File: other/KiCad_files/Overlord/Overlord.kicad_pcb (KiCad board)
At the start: 2 copper layers, 155.7 x 86.3 mm, 230 parts, among them IC1 74HC4052D,653, IC2 74HC4052D,653, IC3 74HC4052D,653, IC4 74HC4052D,653, J1 39502-1011, J2 39502-1011, J3 39502-1011, J4 Conn_01x12_Pin, J5 Conn_01x10_Pin, J6 Conn_01x11_Pin, J7 Conn_01x11_Pin, J8 Conn_01x04_Pin, J9 Conn_01x04_Pin

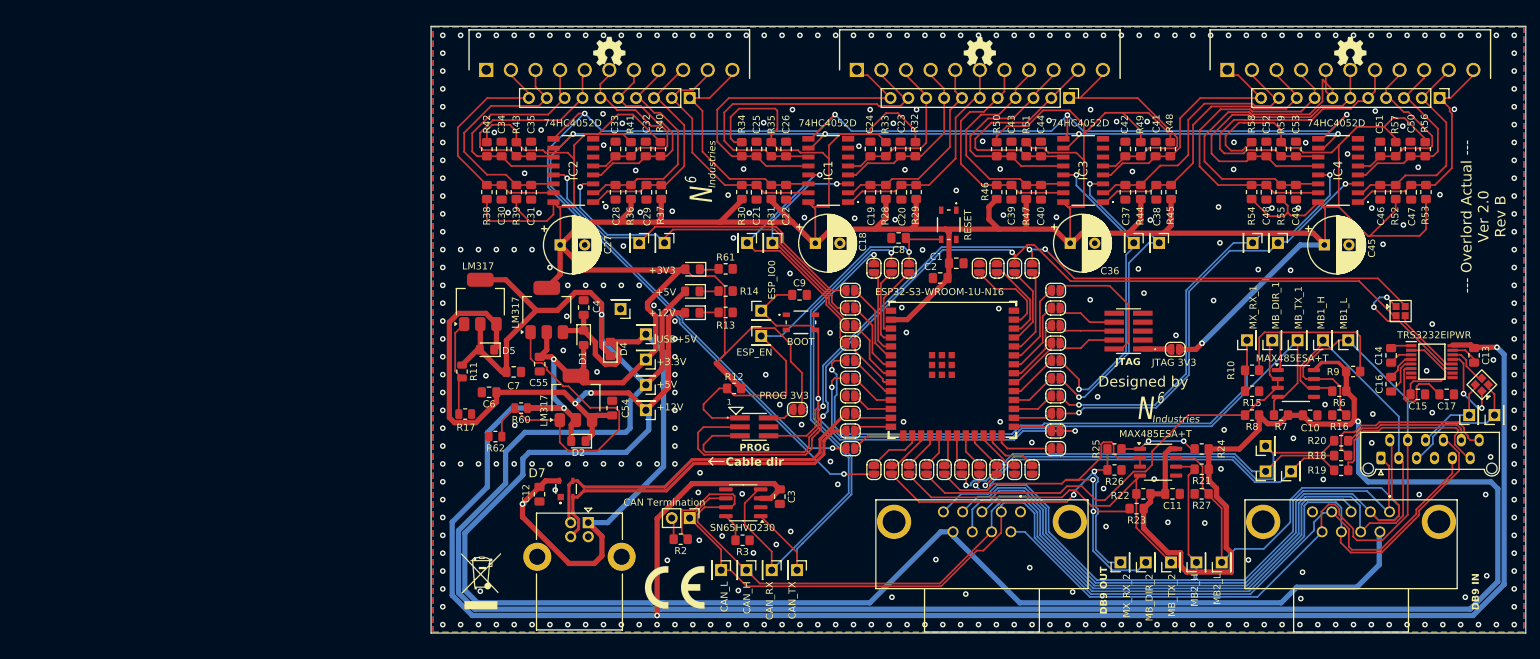
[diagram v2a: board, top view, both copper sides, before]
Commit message: Sent for PCB production, ver 2.1 rev A
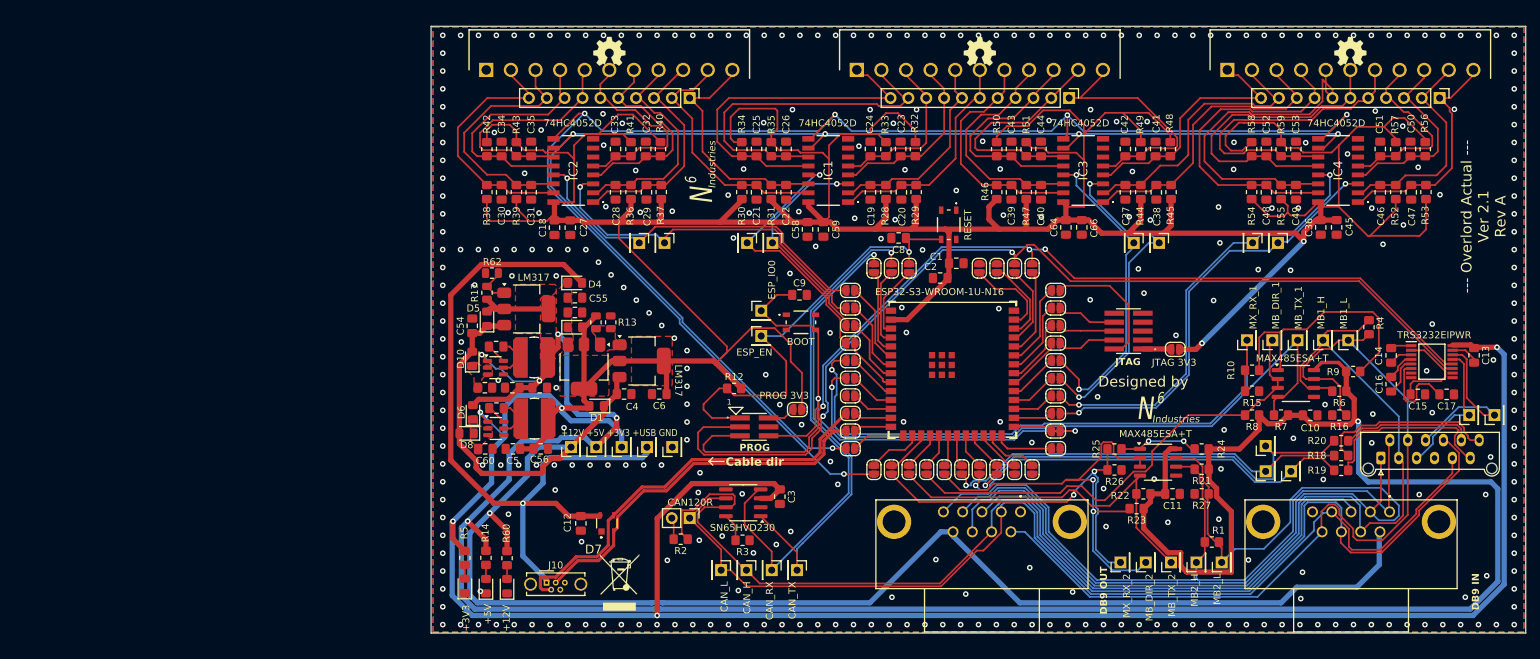
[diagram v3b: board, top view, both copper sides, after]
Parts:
- removed 3V3LED2: LED, LED_SMD:LED_0805_2012Metric_Pad1.15x1.40mm_HandSolder
- removed J8, J9: Conn_01x04_Pin, OverlordCommon:Solder_select_2x2
- removed J_USB1: USB_B, OverlordCommon:USB
- removed R61: 60, Resistor_SMD:R_0805_2012Metric_Pad1.20x1.40mm_HandSolder
- removed SYM7: CE, Symbol:CE-Logo_8.5x6mm_SilkScreen
- added 3V3LED1: LED, LED_SMD:LED_0805_2012Metric_Pad1.15x1.40mm_HandSolder, F.Cu at (29.9, 104.9)
- added C5: 22uF, Capacitor_SMD:C_0805_2012Metric_Pad1.18x1.45mm_HandSolder, F.Cu at (36.7, 85.4)
- added C56: 22uF, Capacitor_SMD:C_0805_2012Metric_Pad1.18x1.45mm_HandSolder, F.Cu at (40.7, 85.4)
- added C57: 0.1uF, Capacitor_SMD:C_0805_2012Metric_Pad1.18x1.45mm_HandSolder, F.Cu at (34.4, 79.6)
- added C58: 0.1uF, Capacitor_SMD:C_0805_2012Metric_Pad1.18x1.45mm_HandSolder, F.Cu at (78.6, 54.2)
- added C59: 10uF, Capacitor_SMD:C_0805_2012Metric_Pad1.18x1.45mm_HandSolder, F.Cu at (80.9, 54.2)
- added C60: 10uF, Capacitor_SMD:C_0805_2012Metric_Pad1.18x1.45mm_HandSolder, F.Cu at (32.8, 85.4)
- added C61: 22uF, Capacitor_SMD:C_0805_2012Metric_Pad1.18x1.45mm_HandSolder, F.Cu at (36.6, 76.7)
- added C62: 22uF, Capacitor_SMD:C_0805_2012Metric_Pad1.18x1.45mm_HandSolder, F.Cu at (40.5, 76.7)
- added C63: 0.1uF, Capacitor_SMD:C_0805_2012Metric_Pad1.18x1.45mm_HandSolder, F.Cu at (34.4, 70.8)
- added C64: 0.1uF, Capacitor_SMD:C_0805_2012Metric_Pad1.18x1.45mm_HandSolder, F.Cu at (115.4, 53.9)
- added C65: 10uF, Capacitor_SMD:C_0805_2012Metric_Pad1.18x1.45mm_HandSolder, F.Cu at (32.8, 76.7)
- added C66: 10uF, Capacitor_SMD:C_0805_2012Metric_Pad1.18x1.45mm_HandSolder, F.Cu at (117.7, 53.9)
- added D10: 1N4148, Diode_SMD:D_0805_2012Metric_Pad1.15x1.40mm_HandSolder, F.Cu at (30.9, 72.6)
- added D6: 1N4148, Diode_SMD:D_0805_2012Metric_Pad1.15x1.40mm_HandSolder, F.Cu at (31.1, 80.2)
- added D8: 1N4148, Diode_SMD:D_0805_2012Metric_Pad1.15x1.40mm_HandSolder, F.Cu at (30.1, 83.2)
- added J10: USB_B_Micro, Connector_USB:USB_Micro-B_Wuerth_614105150721_Vertical_CircularHoles, F.Cu at (41.5, 104.4)
- added L1: 3.9uH, Inductor_SMD:L_Bourns_SDR0604, F.Cu at (39.8, 81.1)
- added L2: 4.7uH, Inductor_SMD:L_Bourns_SDR0604, F.Cu at (39.8, 72.4)
- added R1: 499, Resistor_SMD:R_0805_2012Metric_Pad1.20x1.40mm_HandSolder, F.Cu at (136.2, 98.7)
- added R4: 499, Resistor_SMD:R_0805_2012Metric_Pad1.20x1.40mm_HandSolder, F.Cu at (158.5, 68.1)
- added R5: 60, Resistor_SMD:R_0805_2012Metric_Pad1.20x1.40mm_HandSolder, F.Cu at (29.9, 100.9)
- added U1: AP63203WU, Package_TO_SOT_SMD:TSOT-23-6, F.Cu at (34.3, 82.5)
- added U2: AP63205WU, Package_TO_SOT_SMD:TSOT-23-6, F.Cu at (34.2, 73.8)
- C18, C36: value 220uF -> 0.1uF; footprint Capacitor_THT:CP_Radial_D8.0mm_P3.50mm -> Capacitor_SMD:C_0805_2012Metric_Pad1.18x1.45mm_HandSolder
- C27, C45: value 220uF -> 10uF; footprint Capacitor_THT:CP_Radial_D8.0mm_P3.50mm -> Capacitor_SMD:C_0805_2012Metric_Pad1.18x1.45mm_HandSolder
- R13: value 499 -> 390; footprint Resistor_SMD:R_0805_2012Metric_Pad1.20x1.40mm_HandSolder -> Resistor_SMD:R_0805_2012Metric
- R17: value 680 -> 240
- R60: value 240 -> 499; footprint Resistor_SMD:R_0805_2012Metric -> Resistor_SMD:R_0805_2012Metric_Pad1.20x1.40mm_HandSolder
- R62: value 390 -> 680
- moved 5VLED1 51.2 mm to (32.9, 104.9), turned to 90 degrees
- moved R14 51.0 mm to (32.9, 100.9), turned to -90 degrees
- moved 12VLED1 47.0 mm to (35.9, 104.9), turned to 90 degrees
- moved C18 37.2 mm to (42.6, 53.9), turned to 90 degrees
- moved C36 35.7 mm to (151.6, 53.9), turned to 90 degrees
- moved C6 24.2 mm to (57.5, 77.6)
- moved R62 23.3 mm to (33.8, 60.4)
- moved C54 23.1 mm to (30.9, 67.9)
- moved R60 21.4 mm to (35.9, 101.0), turned to -90 degrees
- moved Dbg19 21.0 mm to (59.4, 85.2), turned to 90 degrees
- moved R11 20.3 mm to (48.5, 67.4)
- moved SYM6 19.7 mm to (51.9, 104.4)
- moved R17 17.5 mm to (33.0, 63.2), turned to 90 degrees
- moved U_LM317_2 17.4 mm to (46.9, 73.7), turned to -90 degrees
- moved R13 16.4 mm to (50.6, 67.4), turned to 90 degrees
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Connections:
- 12VLED1 pad 1: Net-(12VLED1-K) -> GND
- 12VLED1 pad 2: +12V -> Net-(12VLED1-A)
- 5VLED1 pad 1: Net-(5VLED1-K) -> GND
- 5VLED1 pad 2: +5V -> Net-(5VLED1-A)
- C18 pad 1: +3.3V -> GND
- C18 pad 2: GND -> +3.3V
- C27 pad 1: +3.3V -> GND
- C27 pad 2: GND -> +3.3V
- C36 pad 1: +3.3V -> GND
- C36 pad 2: GND -> +3.3V
- C4 pad 1: USB+5V -> +12V
- C45 pad 1: +3.3V -> GND
- C45 pad 2: GND -> +3.3V
- C55 pad 1: +3.3V -> +5V
- C6 pad 1: +12V -> +3.3V
- D1 pad 1: USB+5V -> +12V
- D2 pad 1: +12V -> +5V
- J4 pad 1: MB2_H -> MB2_L
- J4 pad 2: MB2_L -> MB2_H
- R11 pad 1: +5V -> +3.3V
- R11 pad 2: Net-(U_LM317_2-ADJ) -> V_ADJ
- R13 pad 1: Net-(12VLED1-K) -> V_ADJ
- R14 pad 1: Net-(5VLED1-K) -> +5V
- R14 pad 2: GND -> Net-(5VLED1-A)
- R17 pad 1: Net-(U_LM317_2-ADJ) -> +5V
- R17 pad 2: GND -> Net-(U_LM317_3-ADJ)
- R60 pad 1: +3.3V -> +12V
- R60 pad 2: V_ADJ -> Net-(12VLED1-A)
- R62 pad 1: V_ADJ -> Net-(U_LM317_3-ADJ)
- U_LM317_1 pad 3: USB+5V -> +12V
- U_LM317_2 pad 1: Net-(U_LM317_2-ADJ) -> V_ADJ
- U_LM317_2 pad 2: +5V -> +3.3V
- U_LM317_2 pad 3: +12V -> +5V
- U_LM317_3 pad 1: V_ADJ -> Net-(U_LM317_3-ADJ)
- U_LM317_3 pad 2: +3.3V -> +5V
- U_TRS3232EIPWR1 pad 11: Net-(J9-Pin_1) -> UART_TX_0
- U_TRS3232EIPWR1 pad 12: Net-(J9-Pin_2) -> UART_RX_0
- U_TRS3232EIPWR1 pad 13: Net-(J8-Pin_1) -> RS232_TX
- U_TRS3232EIPWR1 pad 14: Net-(J8-Pin_2) -> RS232_RX
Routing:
- net V_ADJ: track 47.5 -> 0.00 mm
- net +12V: track 276.3 -> 236.2 mm, vias 2 -> 1
- net +5V: track 409.7 -> 384.8 mm, vias 2 -> 6
- net USB+5V: track 84.8 -> 105.1 mm
- net Net-(J9-Pin_1): track 19.4 -> 0.00 mm, vias 2 -> 0
- net +3.3V: track 917.8 -> 900.5 mm, vias 5 -> 7
- net Net-(U_LM317_2-ADJ): track 13.9 -> 0.00 mm
- net RS232_RX: track 11.9 -> 24.9 mm
- net Net-(J8-Pin_1): track 11.5 -> 0.00 mm, vias 2 -> 0
- net UART_TX_0: track 133.2 -> 144.3 mm
- net Net-(J9-Pin_2): track 10.2 -> 0.00 mm
- net UART_RX_0: track 129.9 -> 139.9 mm
- net D-: track 50.9 -> 59.4 mm
- net MB1_H: track 128.4 -> 136.5 mm
- net Net-(MAX485ESA+T_1-RO): track 30.1 -> 37.8 mm
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- added copper zone on F.Cu, net +3.3V
- added copper zone on F.Cu, net +5V
- added copper zone on F.Cu, net Net-(D10-K)
- added copper zone on F.Cu, net Net-(D6-K)
- added copper zone on F.Cu, net V_ADJ
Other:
- board text added: "+12V +5V +3V3 +USB GND"
- board text added: "--- Overlord Actual --- Ver 2.1 Rev A"
- board text added: "CAN120R"
- board text removed: "--- Overlord Actual --- Ver 2.0 Rev B"
- board text removed: "CAN Termination"
- board text removed: "USB+5V +3.3V +5V +12V"

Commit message: Fixed PCB - changed modbus H/L to A/B - changed RS485 IC to a cheaper variant, fixed pullup resistors - added pullup on boot pin GPIO0 - removed unused power supplies and rerouted USB+5V for better voltage control - added transient voltage suppresion on digital inputs
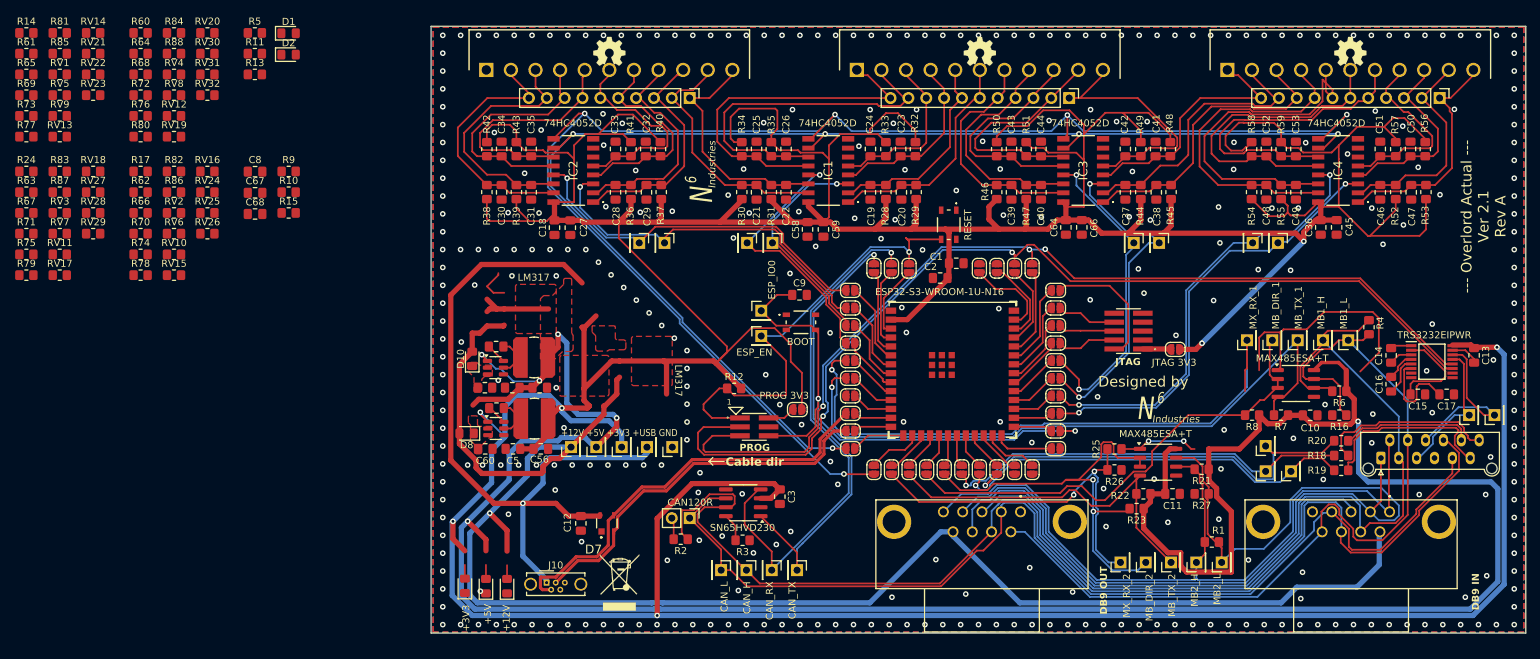
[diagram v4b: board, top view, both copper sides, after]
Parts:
- removed C4, C54, C55, C6, C7: 1uF, Capacitor_SMD:C_0805_2012Metric_Pad1.18x1.45mm_HandSolder
- removed D4: SD0805S020S1R0, Diode_SMD:D_0805_2012Metric_Pad1.15x1.40mm_HandSolder
- removed D5, D6: 1N4148, Diode_SMD:D_0805_2012Metric_Pad1.15x1.40mm_HandSolder
- removed U_LM317_1, U_LM317_2, U_LM317_3: LM317_SOT-223, Package_TO_SOT_SMD:SOT-223-3_TabPin2
- added C67: 10uF, Capacitor_SMD:C_0805_2012Metric_Pad1.18x1.45mm_HandSolder, F.Cu at (0.06, 49.0)
- added C68: 10uF, Capacitor_SMD:C_0805_2012Metric_Pad1.18x1.45mm_HandSolder, F.Cu at (0.06, 52.0)
- added R61: 120, Resistor_SMD:R_0805_2012Metric_Pad1.20x1.40mm_HandSolder, F.Cu at (-32.5, 29.2)
- added R63: 120, Resistor_SMD:R_0805_2012Metric_Pad1.20x1.40mm_HandSolder, F.Cu at (-32.5, 48.9)
- added R64: 120, Resistor_SMD:R_0805_2012Metric_Pad1.20x1.40mm_HandSolder, F.Cu at (-16.2, 29.2)
- added R65: 120, Resistor_SMD:R_0805_2012Metric_Pad1.20x1.40mm_HandSolder, F.Cu at (-32.5, 32.1)
- added R66: 120, Resistor_SMD:R_0805_2012Metric_Pad1.20x1.40mm_HandSolder, F.Cu at (-16.2, 51.8)
- added R67: 120, Resistor_SMD:R_0805_2012Metric_Pad1.20x1.40mm_HandSolder, F.Cu at (-32.5, 51.8)
- added R68: 120, Resistor_SMD:R_0805_2012Metric_Pad1.20x1.40mm_HandSolder, F.Cu at (-16.2, 32.1)
- added R69: 120, Resistor_SMD:R_0805_2012Metric_Pad1.20x1.40mm_HandSolder, F.Cu at (-32.5, 35.1)
- added R70: 120, Resistor_SMD:R_0805_2012Metric_Pad1.20x1.40mm_HandSolder, F.Cu at (-16.2, 54.8)
- added R71: 120, Resistor_SMD:R_0805_2012Metric_Pad1.20x1.40mm_HandSolder, F.Cu at (-32.5, 54.8)
- added R72: 120, Resistor_SMD:R_0805_2012Metric_Pad1.20x1.40mm_HandSolder, F.Cu at (-16.2, 35.1)
- added R73: 120, Resistor_SMD:R_0805_2012Metric_Pad1.20x1.40mm_HandSolder, F.Cu at (-32.5, 38.0)
- added R74: 120, Resistor_SMD:R_0805_2012Metric_Pad1.20x1.40mm_HandSolder, F.Cu at (-16.2, 57.7)
- added R75: 120, Resistor_SMD:R_0805_2012Metric_Pad1.20x1.40mm_HandSolder, F.Cu at (-32.5, 57.7)
- added R76: 120, Resistor_SMD:R_0805_2012Metric_Pad1.20x1.40mm_HandSolder, F.Cu at (-16.2, 38.0)
- added R77: 120, Resistor_SMD:R_0805_2012Metric_Pad1.20x1.40mm_HandSolder, F.Cu at (-32.5, 41.0)
- added R78: 120, Resistor_SMD:R_0805_2012Metric_Pad1.20x1.40mm_HandSolder, F.Cu at (-16.2, 60.7)
- added R79: 120, Resistor_SMD:R_0805_2012Metric_Pad1.20x1.40mm_HandSolder, F.Cu at (-32.5, 60.7)
- added R80: 120, Resistor_SMD:R_0805_2012Metric_Pad1.20x1.40mm_HandSolder, F.Cu at (-16.2, 41.0)
- added R81: 120, Resistor_SMD:R_0805_2012Metric_Pad1.20x1.40mm_HandSolder, F.Cu at (-27.7, 26.2)
- added R82: 120, Resistor_SMD:R_0805_2012Metric_Pad1.20x1.40mm_HandSolder, F.Cu at (-11.5, 45.9)
- added R83: 120, Resistor_SMD:R_0805_2012Metric_Pad1.20x1.40mm_HandSolder, F.Cu at (-27.7, 45.9)
- added R84: 120, Resistor_SMD:R_0805_2012Metric_Pad1.20x1.40mm_HandSolder, F.Cu at (-11.5, 26.2)
- added R85: 120, Resistor_SMD:R_0805_2012Metric_Pad1.20x1.40mm_HandSolder, F.Cu at (-27.7, 29.2)
- added R86: 120, Resistor_SMD:R_0805_2012Metric_Pad1.20x1.40mm_HandSolder, F.Cu at (-11.5, 48.9)
- added R87: 120, Resistor_SMD:R_0805_2012Metric_Pad1.20x1.40mm_HandSolder, F.Cu at (-27.7, 48.9)
- added R88: 120, Resistor_SMD:R_0805_2012Metric_Pad1.20x1.40mm_HandSolder, F.Cu at (-11.5, 29.2)
- added RV1: TVS 3V3, Resistor_SMD:R_0805_2012Metric_Pad1.20x1.40mm_HandSolder, F.Cu at (-27.7, 32.1)
- added RV10: TVS 3V3, Resistor_SMD:R_0805_2012Metric_Pad1.20x1.40mm_HandSolder, F.Cu at (-11.5, 57.7)
- added RV11: TVS 3V3, Resistor_SMD:R_0805_2012Metric_Pad1.20x1.40mm_HandSolder, F.Cu at (-27.7, 57.7)
- added RV12: TVS 3V3, Resistor_SMD:R_0805_2012Metric_Pad1.20x1.40mm_HandSolder, F.Cu at (-11.5, 38.0)
- added RV13: TVS 3V3, Resistor_SMD:R_0805_2012Metric_Pad1.20x1.40mm_HandSolder, F.Cu at (-27.7, 41.0)
- added RV14: TVS 3V3, Resistor_SMD:R_0805_2012Metric_Pad1.20x1.40mm_HandSolder, F.Cu at (-23.0, 26.2)
- added RV15: TVS 3V3, Resistor_SMD:R_0805_2012Metric_Pad1.20x1.40mm_HandSolder, F.Cu at (-11.5, 60.7)
- added RV16: TVS 3V3, Resistor_SMD:R_0805_2012Metric_Pad1.20x1.40mm_HandSolder, F.Cu at (-6.72, 45.9)
- added RV17: TVS 3V3, Resistor_SMD:R_0805_2012Metric_Pad1.20x1.40mm_HandSolder, F.Cu at (-27.7, 60.7)
- added RV18: TVS 3V3, Resistor_SMD:R_0805_2012Metric_Pad1.20x1.40mm_HandSolder, F.Cu at (-23.0, 45.9)
- added RV19: TVS 3V3, Resistor_SMD:R_0805_2012Metric_Pad1.20x1.40mm_HandSolder, F.Cu at (-11.5, 41.0)
- added RV2: TVS 3V3, Resistor_SMD:R_0805_2012Metric_Pad1.20x1.40mm_HandSolder, F.Cu at (-11.5, 51.8)
- added RV20: TVS 3V3, Resistor_SMD:R_0805_2012Metric_Pad1.20x1.40mm_HandSolder, F.Cu at (-6.72, 26.2)
- added RV21: TVS 3V3, Resistor_SMD:R_0805_2012Metric_Pad1.20x1.40mm_HandSolder, F.Cu at (-23.0, 29.2)
- added RV22: TVS 3V3, Resistor_SMD:R_0805_2012Metric_Pad1.20x1.40mm_HandSolder, F.Cu at (-23.0, 32.1)
- added RV23: TVS 3V3, Resistor_SMD:R_0805_2012Metric_Pad1.20x1.40mm_HandSolder, F.Cu at (-23.0, 35.1)
- added RV24: TVS 3V3, Resistor_SMD:R_0805_2012Metric_Pad1.20x1.40mm_HandSolder, F.Cu at (-6.72, 48.9)
- added RV25: TVS 3V3, Resistor_SMD:R_0805_2012Metric_Pad1.20x1.40mm_HandSolder, F.Cu at (-6.72, 51.8)
- added RV26: TVS 3V3, Resistor_SMD:R_0805_2012Metric_Pad1.20x1.40mm_HandSolder, F.Cu at (-6.72, 54.8)
- added RV27: TVS 3V3, Resistor_SMD:R_0805_2012Metric_Pad1.20x1.40mm_HandSolder, F.Cu at (-23.0, 48.9)
- added RV28: TVS 3V3, Resistor_SMD:R_0805_2012Metric_Pad1.20x1.40mm_HandSolder, F.Cu at (-23.0, 51.8)
- added RV29: TVS 3V3, Resistor_SMD:R_0805_2012Metric_Pad1.20x1.40mm_HandSolder, F.Cu at (-23.0, 54.8)
- added RV3: TVS 3V3, Resistor_SMD:R_0805_2012Metric_Pad1.20x1.40mm_HandSolder, F.Cu at (-27.7, 51.8)
- added RV30: TVS 3V3, Resistor_SMD:R_0805_2012Metric_Pad1.20x1.40mm_HandSolder, F.Cu at (-6.72, 29.2)
- added RV31: TVS 3V3, Resistor_SMD:R_0805_2012Metric_Pad1.20x1.40mm_HandSolder, F.Cu at (-6.72, 32.1)
- added RV32: TVS 3V3, Resistor_SMD:R_0805_2012Metric_Pad1.20x1.40mm_HandSolder, F.Cu at (-6.72, 35.1)
- added RV4: TVS 3V3, Resistor_SMD:R_0805_2012Metric_Pad1.20x1.40mm_HandSolder, F.Cu at (-11.5, 32.1)
- added RV5: TVS 3V3, Resistor_SMD:R_0805_2012Metric_Pad1.20x1.40mm_HandSolder, F.Cu at (-27.7, 35.1)
- added RV6: TVS 3V3, Resistor_SMD:R_0805_2012Metric_Pad1.20x1.40mm_HandSolder, F.Cu at (-11.5, 54.8)
- added RV7: TVS 3V3, Resistor_SMD:R_0805_2012Metric_Pad1.20x1.40mm_HandSolder, F.Cu at (-27.7, 54.8)
- added RV8: TVS 3V3, Resistor_SMD:R_0805_2012Metric_Pad1.20x1.40mm_HandSolder, F.Cu at (-11.5, 35.1)
- added RV9: TVS 3V3, Resistor_SMD:R_0805_2012Metric_Pad1.20x1.40mm_HandSolder, F.Cu at (-27.7, 38.0)
- C8: value 0.1uF -> 10uF
- D1, D2: value 1N4148 -> SD0805S020S0R5
- R10: value 3K3 -> 6K8
- R11: value 240 -> 10K; footprint Resistor_SMD:R_0805_2012Metric -> Resistor_SMD:R_0805_2012Metric_Pad1.20x1.40mm_HandSolder
- R13: value 390 -> 3K3; footprint Resistor_SMD:R_0805_2012Metric -> Resistor_SMD:R_0805_2012Metric_Pad1.20x1.40mm_HandSolder
- R14: value 147 -> 120
- R15: value 6K8 -> 10k
- R17: value 240 -> 120; footprint Resistor_SMD:R_0805_2012Metric -> Resistor_SMD:R_0805_2012Metric_Pad1.20x1.40mm_HandSolder
- R24: value 10K -> 120
- R5: value 60 -> 499
- R60: value 499 -> 120
- R62: value 680 -> 120; footprint Resistor_SMD:R_0805_2012Metric -> Resistor_SMD:R_0805_2012Metric_Pad1.20x1.40mm_HandSolder
- R9: value 10K -> 3K3
- SP485EEN-L/TR_1: renamed from MAX485ESA+T_1; value MAX485ESA+T -> SP485EEN-L/TR
- SP485EEN-L/TR_2: renamed from MAX485ESA+T_2; value MAX485ESA+T -> SP485EEN-L/TR
- moved R24 171.8 mm to (-32.5, 45.9), turned to 0 degrees
- moved R9 154.1 mm to (4.84, 45.9)
- moved R15 139.4 mm to (4.84, 51.8), turned to 0 degrees
- moved R10 139.4 mm to (4.84, 48.9)
- moved R14 99.2 mm to (-32.5, 26.2), turned to 0 degrees
- moved C8 92.0 mm to (0.06, 46.0), turned to 0 degrees
- moved R60 91.1 mm to (-16.2, 26.2), turned to 0 degrees
- moved R5 80.4 mm to (0.03, 26.2), turned to 0 degrees
- moved D1 68.8 mm to (4.83, 26.3), turned to 0 degrees
- moved R11 61.8 mm to (0.03, 29.2), turned to 0 degrees
- moved R13 61.7 mm to (0.03, 32.1), turned to 0 degrees
- moved D2 56.2 mm to (4.83, 29.3)
- moved R17 52.2 mm to (-16.2, 45.9), turned to 0 degrees
- moved R62 51.3 mm to (-16.2, 48.9), turned to 0 degrees
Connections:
- C60 pad 2: Net-(D6-K) -> Net-(D1-K)
- D1 pad 1: +12V -> Net-(D1-K)
- D1 pad 2: +3.3V -> USB+5V
- D2 pad 2: +3.3V -> USB+5V
- D8 pad 1: Net-(D6-K) -> Net-(D1-K)
- R10 pad 1: MB_RX_U1 -> GND
- R10 pad 2: Net-(MAX485ESA+T_1-RO) -> MB_RX_U1
- R11 pad 1: +3.3V -> +12V
- R11 pad 2: V_ADJ -> Net-(12VLED1-A)
- R13 pad 1: V_ADJ -> +5V
- R13 pad 2: GND -> Net-(5VLED1-A)
- R14 pad 1: +5V -> Net-(R14-Pad1)
- R14 pad 2: Net-(5VLED1-A) -> 3_2Y3
- R15 pad 1: GND -> ESP_IO0
- R15 pad 2: MB_RX_U1 -> +3.3V
- R17 pad 1: +5V -> Net-(R17-Pad1)
- R17 pad 2: Net-(U_LM317_3-ADJ) -> 4_2Y3
- R22 pad 1: +5V -> +3.3V
- R23 pad 1: +5V -> +3.3V
- R24 pad 1: +5V -> Net-(R24-Pad1)
- R24 pad 2: Net-(MAX485ESA+T_2-RO) -> 2_2Y3
- R25 pad 2: Net-(MAX485ESA+T_2-RO) -> Net-(SP485EEN-L/TR_2-RO)
- R60 pad 1: +12V -> Net-(R60-Pad1)
- R60 pad 2: Net-(12VLED1-A) -> 1_2Y3
- R62 pad 1: Net-(U_LM317_3-ADJ) -> Net-(R62-Pad1)
- R62 pad 2: GND -> 4_2Y2
- R7 pad 1: +5V -> +3.3V
- R8 pad 1: +5V -> +3.3V
- R9 pad 1: +5V -> MB_RX_U1
- R9 pad 2: Net-(MAX485ESA+T_1-RO) -> Net-(SP485EEN-L/TR_1-RO)
- SP485EEN-L/TR_1 pad 1: Net-(MAX485ESA+T_1-RO) -> Net-(SP485EEN-L/TR_1-RO)
- SP485EEN-L/TR_2 pad 1: Net-(MAX485ESA+T_2-RO) -> Net-(SP485EEN-L/TR_2-RO)
- U1 pad 2: Net-(D6-K) -> Net-(D1-K)
- U1 pad 3: Net-(D6-K) -> Net-(D1-K)
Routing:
- net Net-(SP485EEN-L/TR_1-RO): track 0.00 -> 37.8 mm
- net Net-(MAX485ESA+T_1-RO): track 37.8 -> 0.00 mm
- net Net-(SP485EEN-L/TR_2-RO): track 0.00 -> 11.3 mm, vias 0 -> 2
- net Net-(MAX485ESA+T_2-RO): track 11.3 -> 0.00 mm, vias 2 -> 0
- net Net-(U_LM317_3-ADJ): track 5.38 -> 0.00 mm
- net (no net): track 0.00 -> 5.38 mm
- added copper zone on F.Cu, net (none)
- added copper zone on F.Cu, net Net-(D1-K)
- removed copper zone on F.Cu, net Net-(D6-K)
- removed copper zone on F.Cu, net V_ADJ
